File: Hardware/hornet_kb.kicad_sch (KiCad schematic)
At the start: 37 parts, among them J1 Conn_ST_STDC14, J10 USB_C_Receptacle_USB2.0, SW98 SW_Push, U1 nRF52840, Y1 32.768kHz, Y2 32MHz

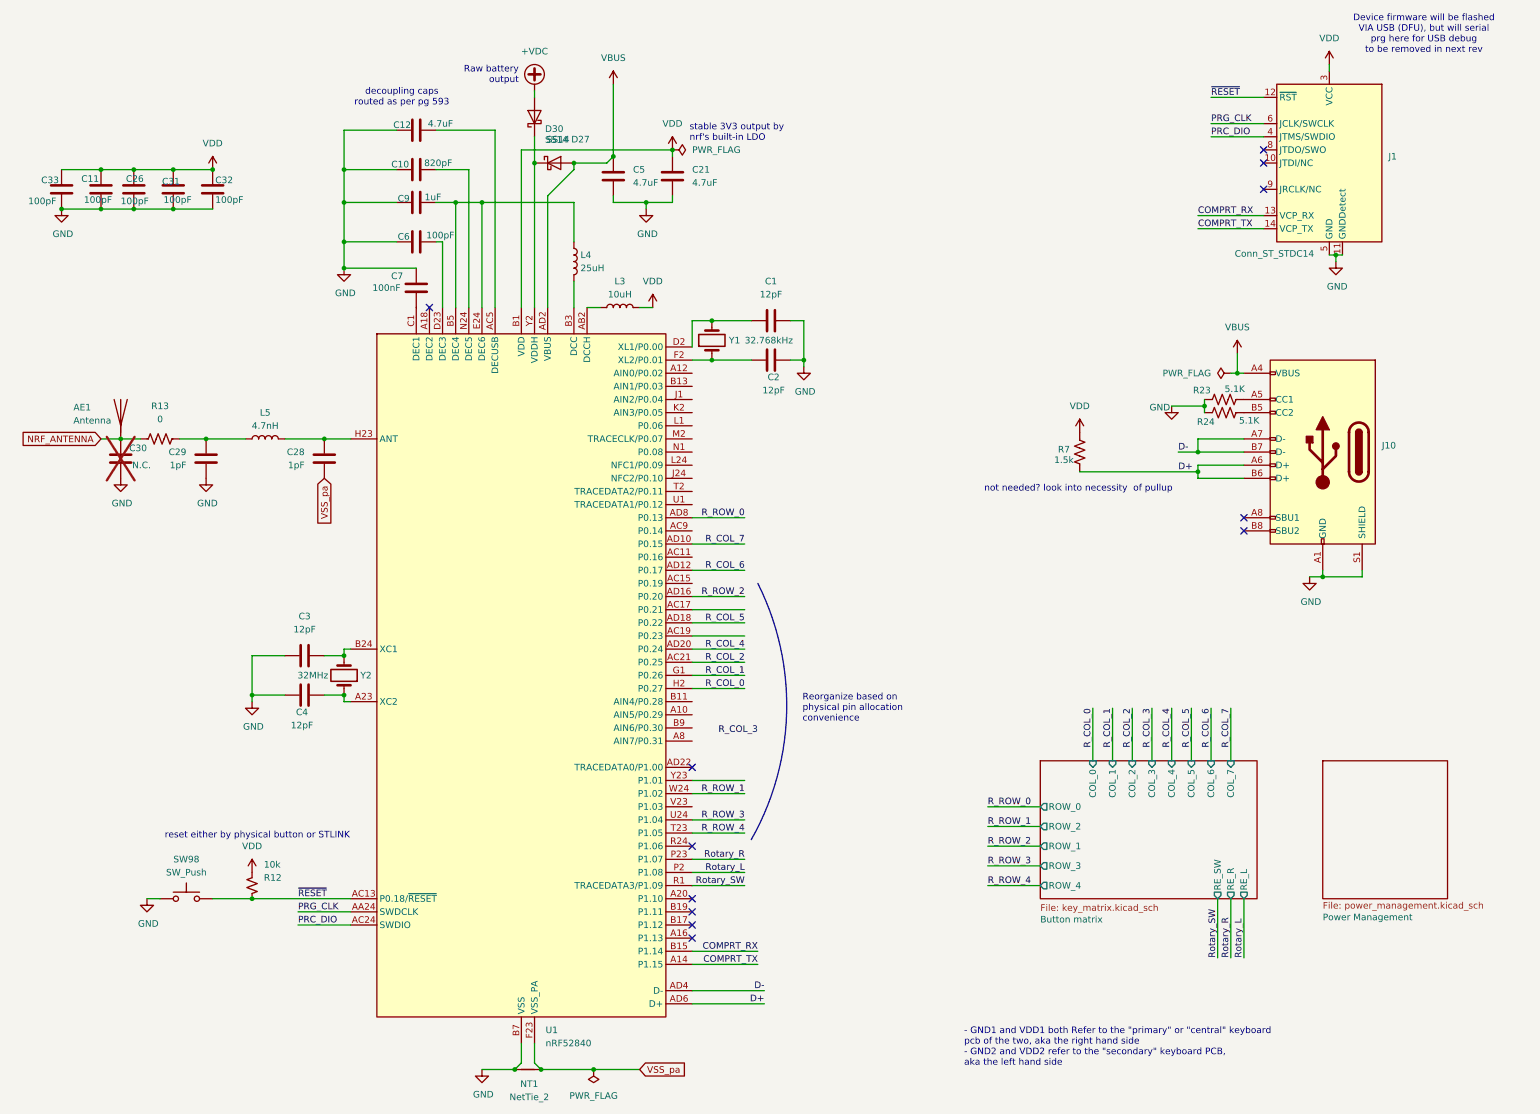
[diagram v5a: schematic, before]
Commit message: added in pwoer mux
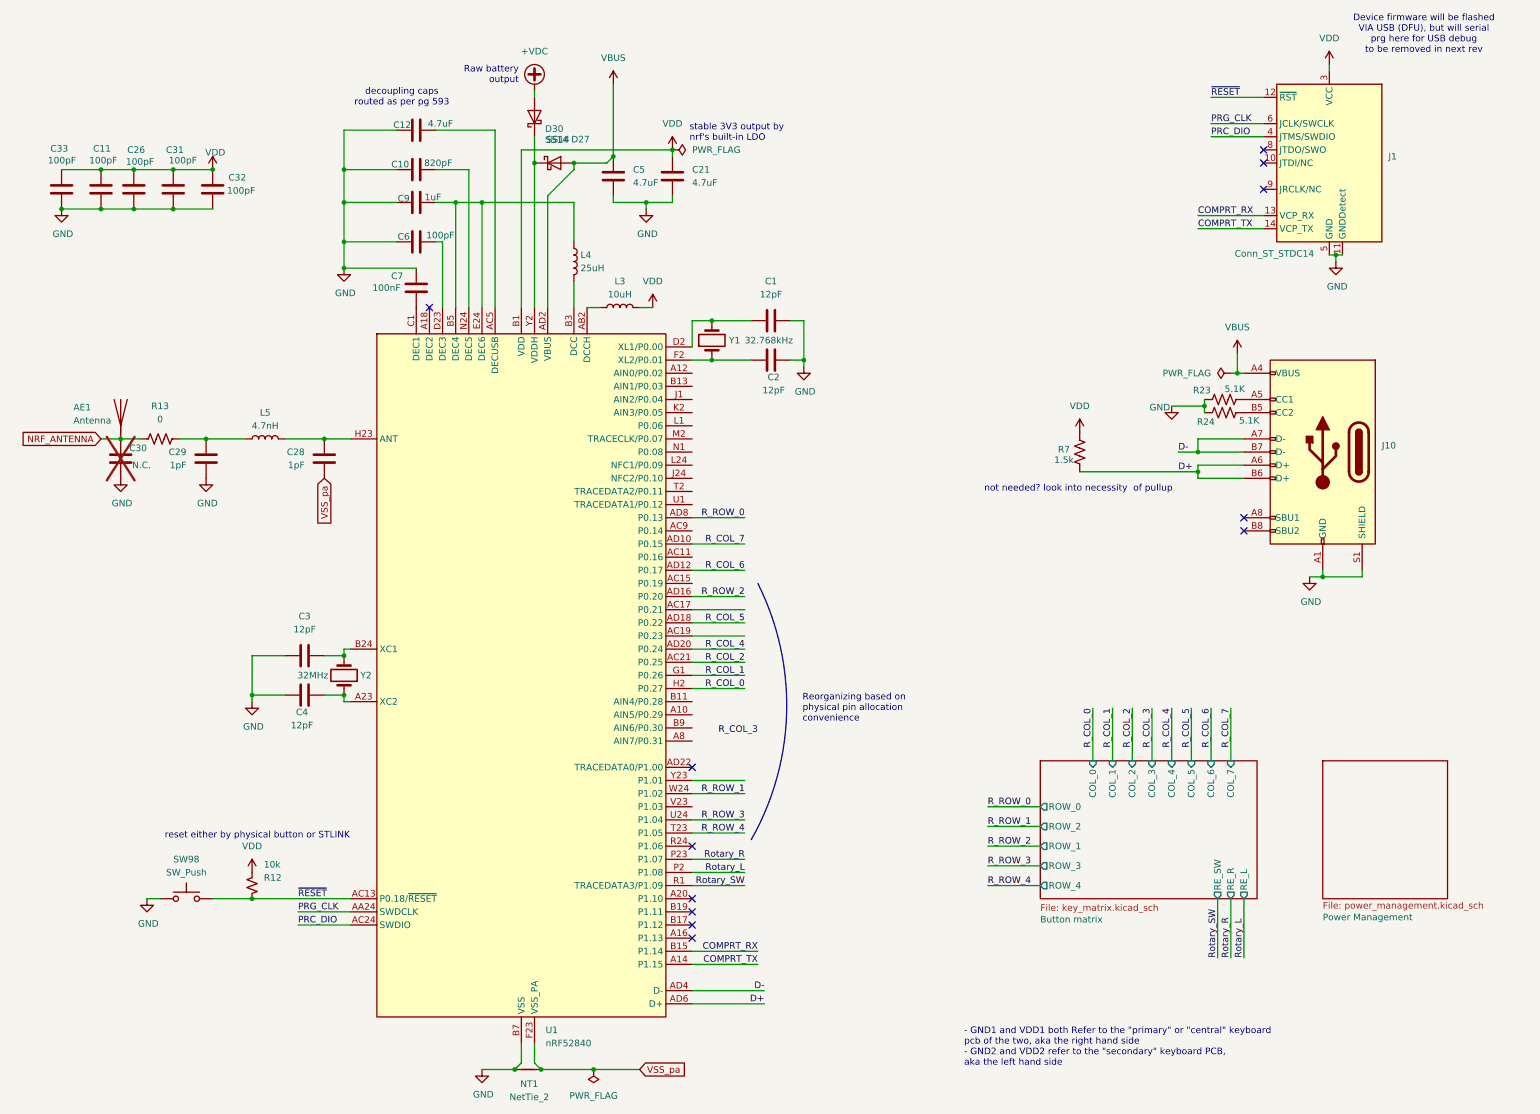
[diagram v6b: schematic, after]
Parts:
- Y2: footprint Crystal:Crystal_SMD_3215-2Pin_3.2x1.5mm -> Crystal:Crystal_SMD_2016-4Pin_2.0x1.6mm; LCSC (none) -> C48332760
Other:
- note added: "Reorganizing based on physical pin allocation convenience"
- note removed: "Reorganize based on physical pin allocation convenience"
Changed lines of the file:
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@@
 		)
 	)
-	(text "Reorganize based on \nphysical pin allocation \nconvenience"
+	(text "Reorganizing based on \nphysical pin allocation \nconvenience"
 		(exclude_from_sim no)
 		(at 171.196 148.59 0)
@@
 		(dnp no)
 		(property "Reference" "C32"
-			(at 57.658 46.482 0)
+			(at 60.198 45.974 0)
 			(effects
 				(font
@@
 		)
 		(property "Value" "100pF"
-			(at 57.658 50.292 0)
+			(at 59.944 48.514 0)
 			(effects
 				(font
@@
 		(on_board yes)
 		(dnp no)
-		(fields_autoplaced yes)
 		(property "Reference" "#PWR027"
 			(at 57.15 48.26 0)
@@
 		)
 		(property "Value" "VDD"
-			(at 57.15 39.37 0)
+			(at 57.658 41.148 0)
 			(effects
 				(font
@@
 		(dnp no)
 		(property "Reference" "C26"
-			(at 40.386 46.228 0)
+			(at 40.64 40.64 0)
 			(effects
 				(font
@@
 		)
 		(property "Value" "100pF"
-			(at 39.37 50.546 0)
+			(at 40.386 42.926 0)
 			(effects
 				(font
@@
 			)
 		)
-		(property "Footprint" "Crystal:Crystal_SMD_3215-2Pin_3.2x1.5mm"
+		(property "Footprint" "Crystal:Crystal_SMD_2016-4Pin_2.0x1.6mm"
 			(at 82.55 142.24 0)
 			(effects
@@
 			)
 		)
+		(property "LCSC" "C48332760"
+			(at 82.55 142.24 90)
+			(effects
+				(font
+					(size 1.27 1.27)
+				)
+				(hide yes)
+			)
+		)
 		(pin "2"
 		)
@@
 		(dnp no)
 		(property "Reference" "C31"
-			(at 50.8 46.736 0)
+			(at 51.562 40.64 0)
 			(effects
 				(font
@@
 		)
 		(property "Value" "100pF"
-			(at 53.086 50.292 0)
+			(at 54.102 42.672 0)
 			(effects
 				(font
@@
 		(dnp no)
 		(property "Reference" "C11"
-			(at 31.75 46.228 0)
+			(at 34.036 40.386 0)
 			(effects
 				(font
@@
 		)
 		(property "Value" "100pF"
-			(at 32.258 50.292 0)
+			(at 33.274 42.672 0)
 			(effects
 				(font
@@
 		(dnp no)
 		(property "Reference" "C33"
-			(at 27.432 46.482 0)
+			(at 29.21 40.386 0)
 			(effects
 				(font
@@
 		)
 		(property "Value" "100pF"
-			(at 26.924 50.546 0)
+			(at 30.734 42.672 0)
 			(effects
 				(font

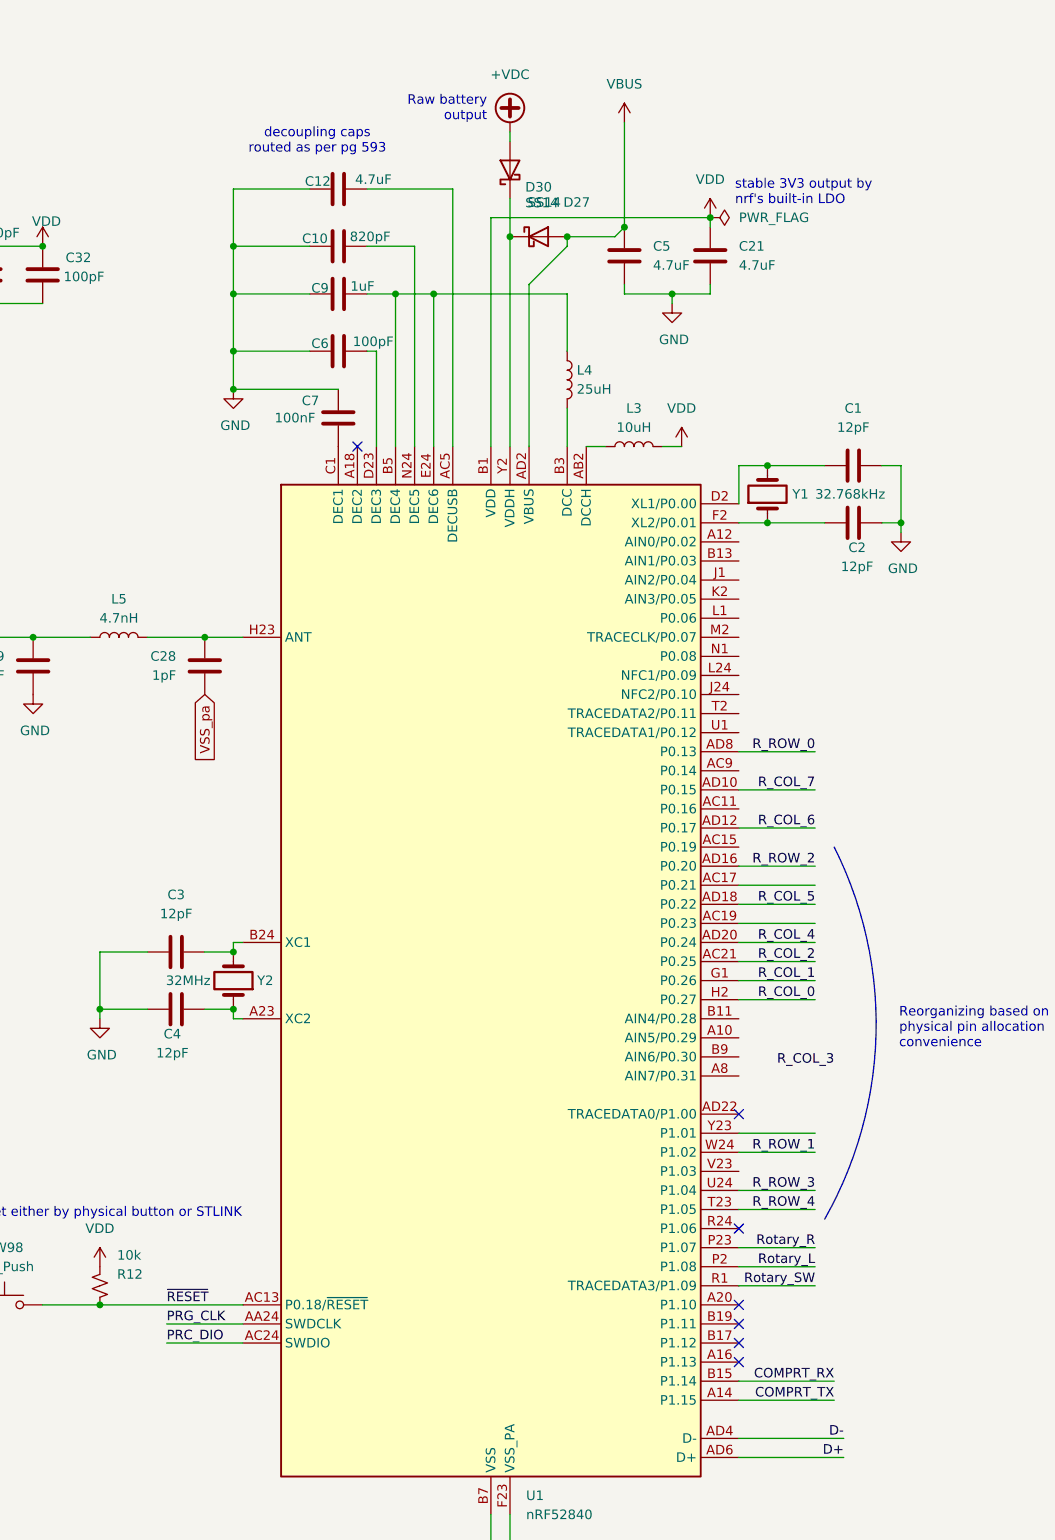
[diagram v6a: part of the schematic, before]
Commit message: modified layout placement
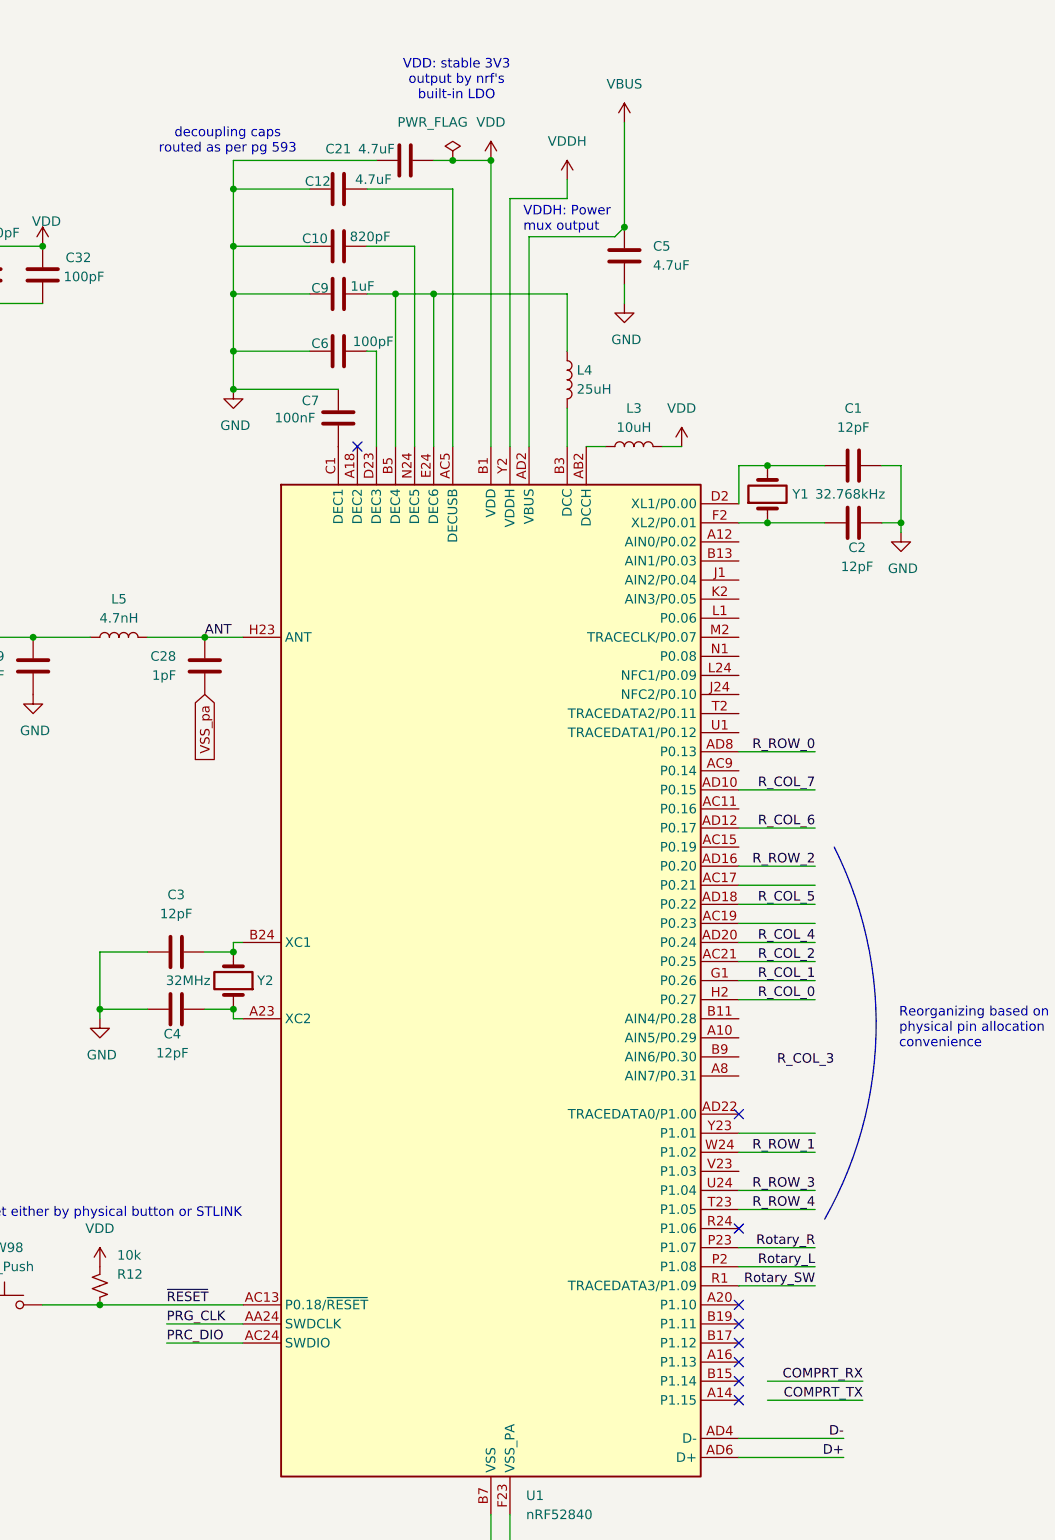
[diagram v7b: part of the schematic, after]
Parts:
- removed D27, D30: SS14, Diode_SMD:D_SMA, symbol Diode:SS14
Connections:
- net COMPRT_RX: no longer U1.B15 (P1.14)
- net COMPRT_TX: no longer U1.A14 (P1.15)
- net GND: now also C21.1; no longer C21.2
- net VDD: now also C21.2; no longer C21.1
- net VDDH: now reaches U1.Y2 (VDDH)
- net ANT: now reaches C28.1, L5.1, U1.H23 (ANT)
- no-connect marks 12 -> 14
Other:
- note added: "VDD: stable 3V3 output by nrf's built-in LDO"
- note added: "VDDH: Power mux output"
- note removed: "Raw battery output"
- note removed: "stable 3V3 output by nrf's built-in LDO"
- moved on the sheet: C21
